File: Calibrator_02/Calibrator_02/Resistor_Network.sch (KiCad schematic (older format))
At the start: 61 parts, among them J6 Conn_Coaxial, U11 KAQY214STLD, U12 KAQY214STLD, U13 KAQY214STLD, U14 KAQY214STLD, U15 KAQY214STLD, U16 KAQY214STLD, U17 KAQY214STLD, U18 KAQY214STLD, U19 KAQY214STLD, U20 KAQY214STLD, U21 KAQY214STLD, U22 KAQY214STLD, U23 KAQY214STLD, U24 KAQY214STLD, U25 KAQY214STLD, U26 KAQY214STLD, U27 KAQY214STLD, U28 KAQY214STLD, U29 KAQY214STLD, U30 KAQY214STLD, U31 KAQY214STLD, U32 KAQY214STLD, U33 KAQY214STLD, U34 KAQY214STLD

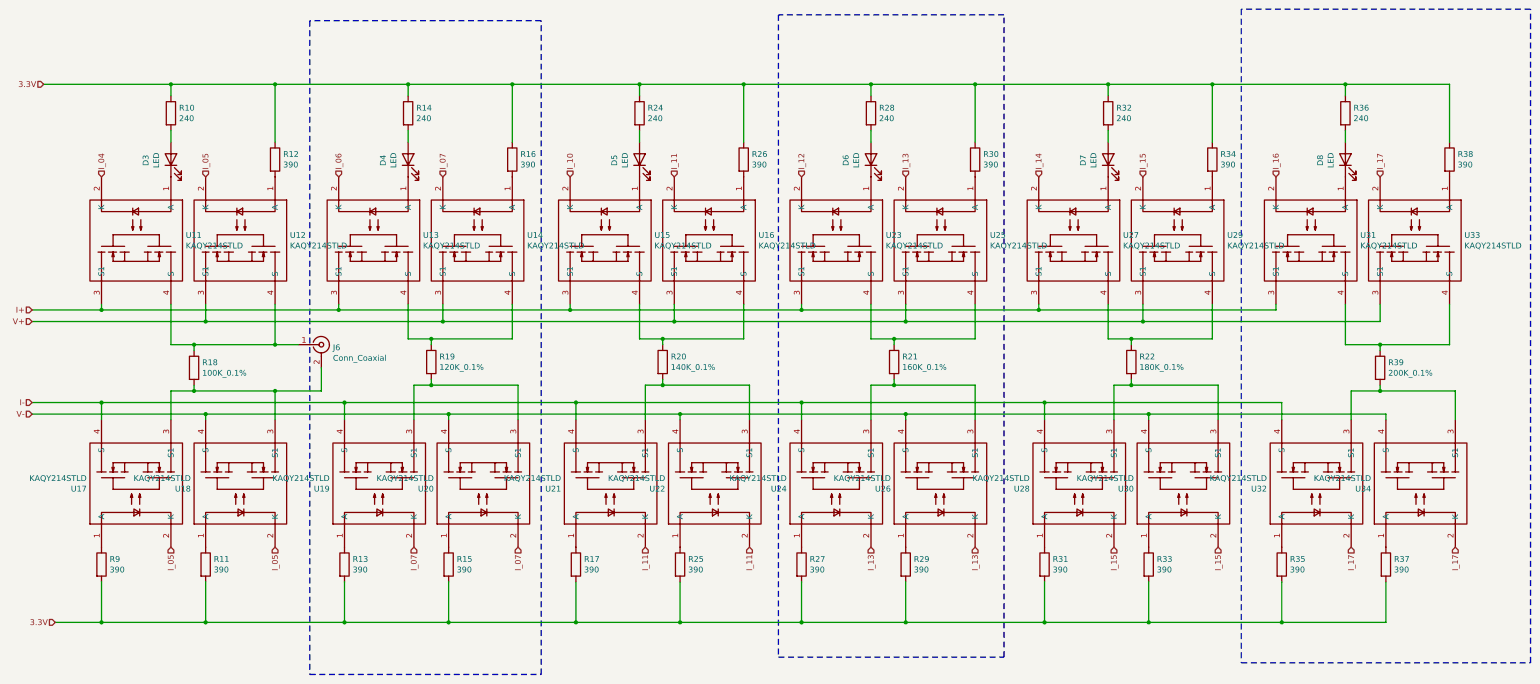
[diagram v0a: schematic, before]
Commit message: Fixed jst pinouts and made Cali board
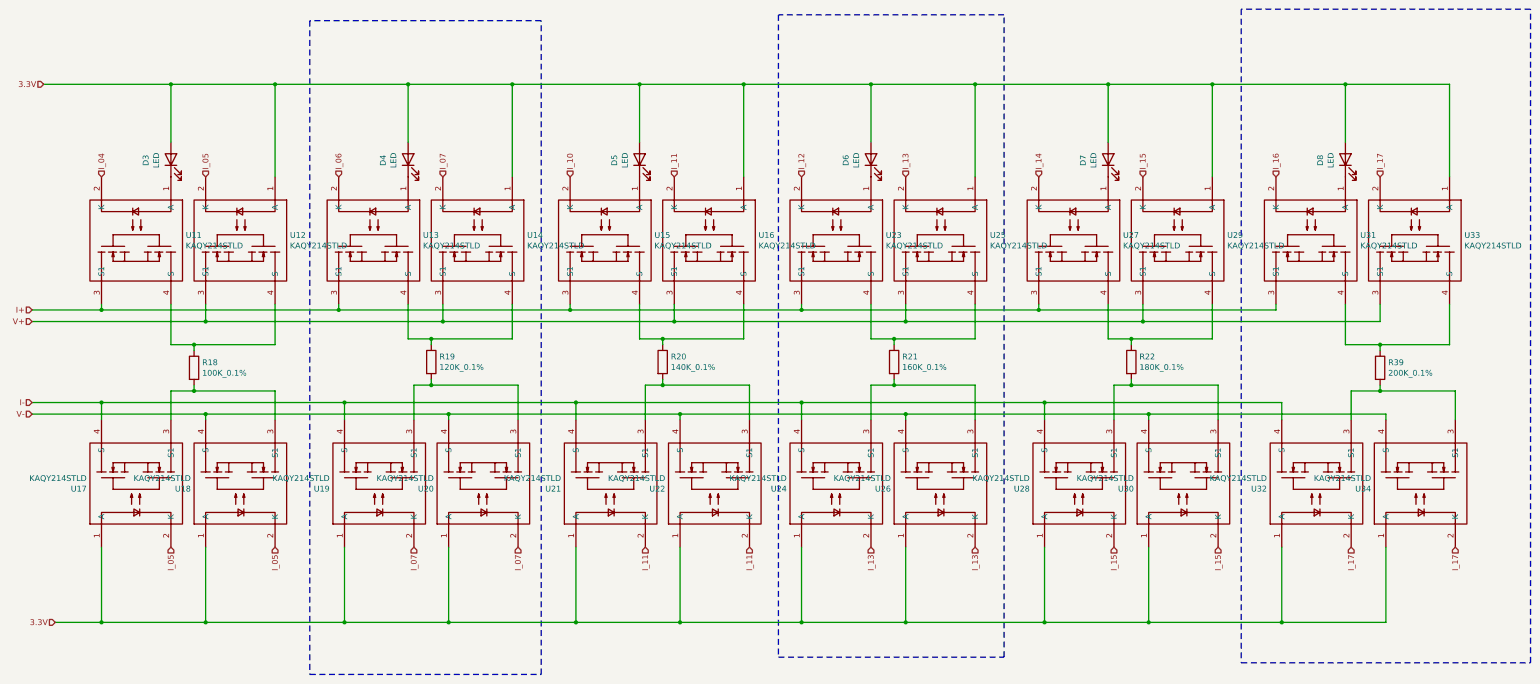
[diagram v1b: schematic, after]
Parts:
- removed J6: Conn_Coaxial, Connector_Coaxial:SMA_Amphenol_132134-10_Vertical, symbol Connector:Conn_Coaxial
- removed R10, R14, R24, R28, R32, R36: 240, Resistor_SMD:R_0402_1005Metric, symbol Device:R
- removed R11, R12, R13, R15, R16, R17, R25, R26, R27, R29, R30, R31, R33, R34, R35, R37, R38, R9: 390, Resistor_SMD:R_0603_1608Metric, symbol Device:R
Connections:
- net 3.3V: now also D3.2 (A), D4.2 (A), D5.2 (A), D6.2 (A), D7.2 (A), D8.2 (A), U12.1 (A), U14.1 (A), U16.1 (A), U17.1 (A), U18.1 (A), U19.1 (A), U20.1 (A), U21.1 (A), U22.1 (A), U24.1 (A), U25.1 (A), U26.1 (A), U28.1 (A), U29.1 (A), U30.1 (A), U32.1 (A), U33.1 (A), U34.1 (A)

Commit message: Update
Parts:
- renumbered R19 to R4, R20 to R5, R21 to R6, R22 to R7, R18 to R8, R39 to R9, U12 to U10, U13 to U11, U14 to U12, U15 to U13, U16 to U14, U23 to U15, U25 to U16, U27 to U17, U29 to U18, U31 to U19, U33 to U20, U17 to U21, U18 to U22, U19 to U23, U20 to U24, U21 to U25, U22 to U26, U24 to U27, U26 to U28, U28 to U29, U32 to U31, U34 to U32, U11 to U9
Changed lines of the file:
@@
 I_06
 $Comp
-L 0_Resistor02:KAQY214STLD U12
+L 0_Resistor02:KAQY214STLD U10
 U 1 1 62893971
 P 2450 2150
-F 0 "U12" V 2404 2578 50  0000 L CNN
+F 0 "U10" V 2404 2578 50  0000 L CNN
 F 1 "KAQY214STLD" V 2495 2578 50  0000 L CNN
 F 2 "0_Resistor_02:SOP-4_L3.9-W4.4-P2.54-LS7.0-BR" H 2450 2455 50  0001 C CNN
@@
 $EndComp
 $Comp
-L 0_Resistor02:KAQY214STLD U13
+L 0_Resistor02:KAQY214STLD U11
 U 1 1 62894BC4
 P 3600 2150
-F 0 "U13" V 3554 2578 50  0000 L CNN
+F 0 "U11" V 3554 2578 50  0000 L CNN
 F 1 "KAQY214STLD" V 3645 2578 50  0000 L CNN
 F 2 "0_Resistor_02:SOP-4_L3.9-W4.4-P2.54-LS7.0-BR" H 3600 2455 50  0001 C CNN
@@
 $EndComp
 $Comp
-L 0_Resistor02:KAQY214STLD U14
+L 0_Resistor02:KAQY214STLD U12
 U 1 1 6289536E
 P 4500 2150
-F 0 "U14" V 4454 2578 50  0000 L CNN
+F 0 "U12" V 4454 2578 50  0000 L CNN
 F 1 "KAQY214STLD" V 4545 2578 50  0000 L CNN
 F 2 "0_Resistor_02:SOP-4_L3.9-W4.4-P2.54-LS7.0-BR" H 4500 2455 50  0001 C CNN
@@
 $EndComp
 $Comp
-L 0_Resistor02:KAQY214STLD U16
+L 0_Resistor02:KAQY214STLD U14
 U 1 1 62898241
 P 6500 2150
-F 0 "U16" V 6454 2578 50  0000 L CNN
+F 0 "U14" V 6454 2578 50  0000 L CNN
 F 1 "KAQY214STLD" V 6545 2578 50  0000 L CNN
 F 2 "0_Resistor_02:SOP-4_L3.9-W4.4-P2.54-LS7.0-BR" H 6500 2455 50  0001 C CNN
@@
 $EndComp
 $Comp
-L 0_Resistor02:KAQY214STLD U15
+L 0_Resistor02:KAQY214STLD U13
 U 1 1 6289ADD7
 P 5600 2150
-F 0 "U15" V 5554 2578 50  0000 L CNN
+F 0 "U13" V 5554 2578 50  0000 L CNN
 F 1 "KAQY214STLD" V 5645 2578 50  0000 L CNN
 F 2 "0_Resistor_02:SOP-4_L3.9-W4.4-P2.54-LS7.0-BR" H 5600 2455 50  0001 C CNN
@@
 V-
 $Comp
-L 0_Resistor02:KAQY214STLD U17
+L 0_Resistor02:KAQY214STLD U21
 U 1 1 628C2DB7
 P 1550 4250
-F 0 "U17" V 1504 4678 50  0000 L CNN
+F 0 "U21" V 1504 4678 50  0000 L CNN
 F 1 "KAQY214STLD" V 1595 4678 50  0000 L CNN
 F 2 "0_Resistor_02:SOP-4_L3.9-W4.4-P2.54-LS7.0-BR" H 1550 4555 50  0001 C CNN
@@
 $EndComp
 $Comp
-L 0_Resistor02:KAQY214STLD U18
+L 0_Resistor02:KAQY214STLD U22
 U 1 1 628DB7E0
 P 2450 4250
-F 0 "U18" V 2404 4678 50  0000 L CNN
+F 0 "U22" V 2404 4678 50  0000 L CNN
 F 1 "KAQY214STLD" V 2495 4678 50  0000 L CNN
 F 2 "0_Resistor_02:SOP-4_L3.9-W4.4-P2.54-LS7.0-BR" H 2450 4555 50  0001 C CNN
@@
 $EndComp
 $Comp
-L 0_Resistor02:KAQY214STLD U25
+L 0_Resistor02:KAQY214STLD U16
 U 1 1 629247FB
 P 8500 2150
-F 0 "U25" V 8454 2578 50  0000 L CNN
+F 0 "U16" V 8454 2578 50  0000 L CNN
 F 1 "KAQY214STLD" V 8545 2578 50  0000 L CNN
 F 2 "0_Resistor_02:SOP-4_L3.9-W4.4-P2.54-LS7.0-BR" H 8500 2455 50  0001 C CNN
@@
 $EndComp
 $Comp
-L 0_Resistor02:KAQY214STLD U23
+L 0_Resistor02:KAQY214STLD U15
 U 1 1 62924803
 P 7600 2150
-F 0 "U23" V 7554 2578 50  0000 L CNN
+F 0 "U15" V 7554 2578 50  0000 L CNN
 F 1 "KAQY214STLD" V 7645 2578 50  0000 L CNN
 F 2 "0_Resistor_02:SOP-4_L3.9-W4.4-P2.54-LS7.0-BR" H 7600 2455 50  0001 C CNN
@@
 $EndComp
 $Comp
-L 0_Resistor02:KAQY214STLD U29
+L 0_Resistor02:KAQY214STLD U18
 U 1 1 6292807F
 P 10550 2150
-F 0 "U29" V 10504 2578 50  0000 L CNN
+F 0 "U18" V 10504 2578 50  0000 L CNN
 F 1 "KAQY214STLD" V 10595 2578 50  0000 L CNN
 F 2 "0_Resistor_02:SOP-4_L3.9-W4.4-P2.54-LS7.0-BR" H 10550 2455 50  0001 C CNN
@@
 $EndComp
 $Comp
-L 0_Resistor02:KAQY214STLD U27
+L 0_Resistor02:KAQY214STLD U17
 U 1 1 62928087
 P 9650 2150
-F 0 "U27" V 9604 2578 50  0000 L CNN
+F 0 "U17" V 9604 2578 50  0000 L CNN
 F 1 "KAQY214STLD" V 9695 2578 50  0000 L CNN
 F 2 "0_Resistor_02:SOP-4_L3.9-W4.4-P2.54-LS7.0-BR" H 9650 2455 50  0001 C CNN
@@
 $EndComp
 $Comp
-L 0_Resistor02:KAQY214STLD U19
+L 0_Resistor02:KAQY214STLD U23
 U 1 1 62952522
 P 3650 4250
-F 0 "U19" V 3604 4678 50  0000 L CNN
+F 0 "U23" V 3604 4678 50  0000 L CNN
 F 1 "KAQY214STLD" V 3695 4678 50  0000 L CNN
 F 2 "0_Resistor_02:SOP-4_L3.9-W4.4-P2.54-LS7.0-BR" H 3650 4555 50  0001 C CNN
@@
 $EndComp
 $Comp
-L 0_Resistor02:KAQY214STLD U20
+L 0_Resistor02:KAQY214STLD U24
 U 1 1 6295252A
 P 4550 4250
-F 0 "U20" V 4504 4678 50  0000 L CNN
+F 0 "U24" V 4504 4678 50  0000 L CNN
 F 1 "KAQY214STLD" V 4595 4678 50  0000 L CNN
 F 2 "0_Resistor_02:SOP-4_L3.9-W4.4-P2.54-LS7.0-BR" H 4550 4555 50  0001 C CNN
@@
 $EndComp
 $Comp
-L 0_Resistor02:KAQY214STLD U21
+L 0_Resistor02:KAQY214STLD U25
 U 1 1 6295A4E4
 P 5650 4250
-F 0 "U21" V 5604 4678 50  0000 L CNN
+F 0 "U25" V 5604 4678 50  0000 L CNN
 F 1 "KAQY214STLD" V 5695 4678 50  0000 L CNN
 F 2 "0_Resistor_02:SOP-4_L3.9-W4.4-P2.54-LS7.0-BR" H 5650 4555 50  0001 C CNN
@@
 $EndComp
 $Comp
-L 0_Resistor02:KAQY214STLD U22
+L 0_Resistor02:KAQY214STLD U26
 U 1 1 6295A4EC
 P 6550 4250
-F 0 "U22" V 6504 4678 50  0000 L CNN
+F 0 "U26" V 6504 4678 50  0000 L CNN
 F 1 "KAQY214STLD" V 6595 4678 50  0000 L CNN
 F 2 "0_Resistor_02:SOP-4_L3.9-W4.4-P2.54-LS7.0-BR" H 6550 4555 50  0001 C CNN
@@
 $EndComp
 $Comp
-L 0_Resistor02:KAQY214STLD U24
+L 0_Resistor02:KAQY214STLD U27
 U 1 1 6296491F
 P 7600 4250
-F 0 "U24" V 7554 4678 50  0000 L CNN
+F 0 "U27" V 7554 4678 50  0000 L CNN
 F 1 "KAQY214STLD" V 7645 4678 50  0000 L CNN
 F 2 "0_Resistor_02:SOP-4_L3.9-W4.4-P2.54-LS7.0-BR" H 7600 4555 50  0001 C CNN
@@
 $EndComp
 $Comp
-L 0_Resistor02:KAQY214STLD U26
+L 0_Resistor02:KAQY214STLD U28
 U 1 1 62964927
 P 8500 4250
-F 0 "U26" V 8454 4678 50  0000 L CNN
+F 0 "U28" V 8454 4678 50  0000 L CNN
 F 1 "KAQY214STLD" V 8545 4678 50  0000 L CNN
 F 2 "0_Resistor_02:SOP-4_L3.9-W4.4-P2.54-LS7.0-BR" H 8500 4555 50  0001 C CNN
@@
 $EndComp
 $Comp
-L 0_Resistor02:KAQY214STLD U28
+L 0_Resistor02:KAQY214STLD U29
 U 1 1 62969201
 P 9700 4250
-F 0 "U28" V 9654 4678 50  0000 L CNN
+F 0 "U29" V 9654 4678 50  0000 L CNN
 F 1 "KAQY214STLD" V 9745 4678 50  0000 L CNN
 F 2 "0_Resistor_02:SOP-4_L3.9-W4.4-P2.54-LS7.0-BR" H 9700 4555 50  0001 C CNN
@@
 Connection ~ 7300 2750
 $Comp
-L 0_Resistor02:KAQY214STLD U33
+L 0_Resistor02:KAQY214STLD U20
 U 1 1 62985DC3
 P 12600 2150
-F 0 "U33" V 12554 2578 50  0000 L CNN
+F 0 "U20" V 12554 2578 50  0000 L CNN
 F 1 "KAQY214STLD" V 12645 2578 50  0000 L CNN
 F 2 "0_Resistor_02:SOP-4_L3.9-W4.4-P2.54-LS7.0-BR" H 12600 2455 50  0001 C CNN
@@
 $EndComp
 $Comp
-L 0_Resistor02:KAQY214STLD U31
+L 0_Resistor02:KAQY214STLD U19
 U 1 1 62985DCB
 P 11700 2150
-F 0 "U31" V 11654 2578 50  0000 L CNN
+F 0 "U19" V 11654 2578 50  0000 L CNN
 F 1 "KAQY214STLD" V 11745 2578 50  0000 L CNN
 F 2 "0_Resistor_02:SOP-4_L3.9-W4.4-P2.54-LS7.0-BR" H 11700 2455 50  0001 C CNN
@@
 $EndComp
 $Comp
-L 0_Resistor02:KAQY214STLD U32
+L 0_Resistor02:KAQY214STLD U31
 U 1 1 62985DF2
 P 11750 4250
-F 0 "U32" V 11704 4678 50  0000 L CNN
+F 0 "U31" V 11704 4678 50  0000 L CNN
 F 1 "KAQY214STLD" V 11795 4678 50  0000 L CNN
 F 2 "0_Resistor_02:SOP-4_L3.9-W4.4-P2.54-LS7.0-BR" H 11750 4555 50  0001 C CNN
@@
 $EndComp
 $Comp
-L 0_Resistor02:KAQY214STLD U34
+L 0_Resistor02:KAQY214STLD U32
 U 1 1 62985DFA
 P 12650 4250
-F 0 "U34" V 12604 4678 50  0000 L CNN
+F 0 "U32" V 12604 4678 50  0000 L CNN
 F 1 "KAQY214STLD" V 12695 4678 50  0000 L CNN
 F 2 "0_Resistor_02:SOP-4_L3.9-W4.4-P2.54-LS7.0-BR" H 12650 4555 50  0001 C CNN
@@
 	11400 2750 11400 2700
 $Comp
-L 0_Resistor02:KAQY214STLD U11
+L 0_Resistor02:KAQY214STLD U9
 U 1 1 6288E641
 P 1550 2150
-F 0 "U11" V 1504 2578 50  0000 L CNN
+F 0 "U9" V 1504 2578 50  0000 L CNN
 F 1 "KAQY214STLD" V 1595 2578 50  0000 L CNN
 F 2 "0_Resistor_02:SOP-4_L3.9-W4.4-P2.54-LS7.0-BR" H 1550 2455 50  0001 C CNN
@@
 $EndComp
 $Comp
-L Device:R R39
+L Device:R R9
 U 1 1 6298B64E
 P 12300 3250
-F 0 "R39" H 12370 3296 50  0000 L CNN
+F 0 "R9" H 12370 3296 50  0000 L CNN
 F 1 "200K_0.1%" H 12370 3205 50  0000 L CNN
 F 2 "Resistor_SMD:R_0603_1608Metric_Pad0.98x0.95mm_HandSolder" V 12230 3250 50  0001 C CNN
@@
 	12300 3450 12950 3450
 $Comp
-L Device:R R22
+L Device:R R7
 U 1 1 6299B156
 P 10150 3200
-F 0 "R22" H 10220 3246 50  0000 L CNN
+F 0 "R7" H 10220 3246 50  0000 L CNN
 F 1 "180K_0.1%" H 10220 3155 50  0000 L CNN
 F 2 "Resistor_SMD:R_0805_2012Metric_Pad1.20x1.40mm_HandSolder" V 10080 3200 50  0001 C CNN
@@
 	10150 3400 10900 3400
 $Comp
-L Device:R R21
+L Device:R R6
 U 1 1 629A9E7C
 P 8100 3200
-F 0 "R21" H 8170 3246 50  0000 L CNN
+F 0 "R6" H 8170 3246 50  0000 L CNN
 F 1 "160K_0.1%" H 8170 3155 50  0000 L CNN
 F 2 "Resistor_SMD:R_0805_2012Metric_Pad1.20x1.40mm_HandSolder" V 8030 3200 50  0001 C CNN
@@
 	8100 3400 8800 3400
 $Comp
-L Device:R R20
+L Device:R R5
 U 1 1 629B9198
 P 6100 3200
-F 0 "R20" H 6170 3246 50  0000 L CNN
+F 0 "R5" H 6170 3246 50  0000 L CNN
 F 1 "140K_0.1%" H 6170 3155 50  0000 L CNN
 F 2 "Resistor_SMD:R_0603_1608Metric_Pad0.98x0.95mm_HandSolder" V 6030 3200 50  0001 C CNN
@@
 	6100 3400 6850 3400
 $Comp
-L Device:R R19
+L Device:R R4
 U 1 1 629C927A
 P 4100 3200
-F 0 "R19" H 4170 3246 50  0000 L CNN
+F 0 "R4" H 4170 3246 50  0000 L CNN
 F 1 "120K_0.1%" H 4170 3155 50  0000 L CNN
 F 2 "Resistor_SMD:R_0603_1608Metric_Pad0.98x0.95mm_HandSolder" V 4030 3200 50  0001 C CNN
@@
 	4100 3400 4850 3400
 $Comp
-L Device:R R18
+L Device:R R8
 U 1 1 629D9115
 P 2050 3250
-F 0 "R18" H 2120 3296 50  0000 L CNN
+F 0 "R8" H 2120 3296 50  0000 L CNN
 F 1 "100K_0.1%" H 2120 3205 50  0000 L CNN
 F 2 "Resistor_SMD:R_0603_1608Metric_Pad0.98x0.95mm_HandSolder" V 1980 3250 50  0001 C CNN

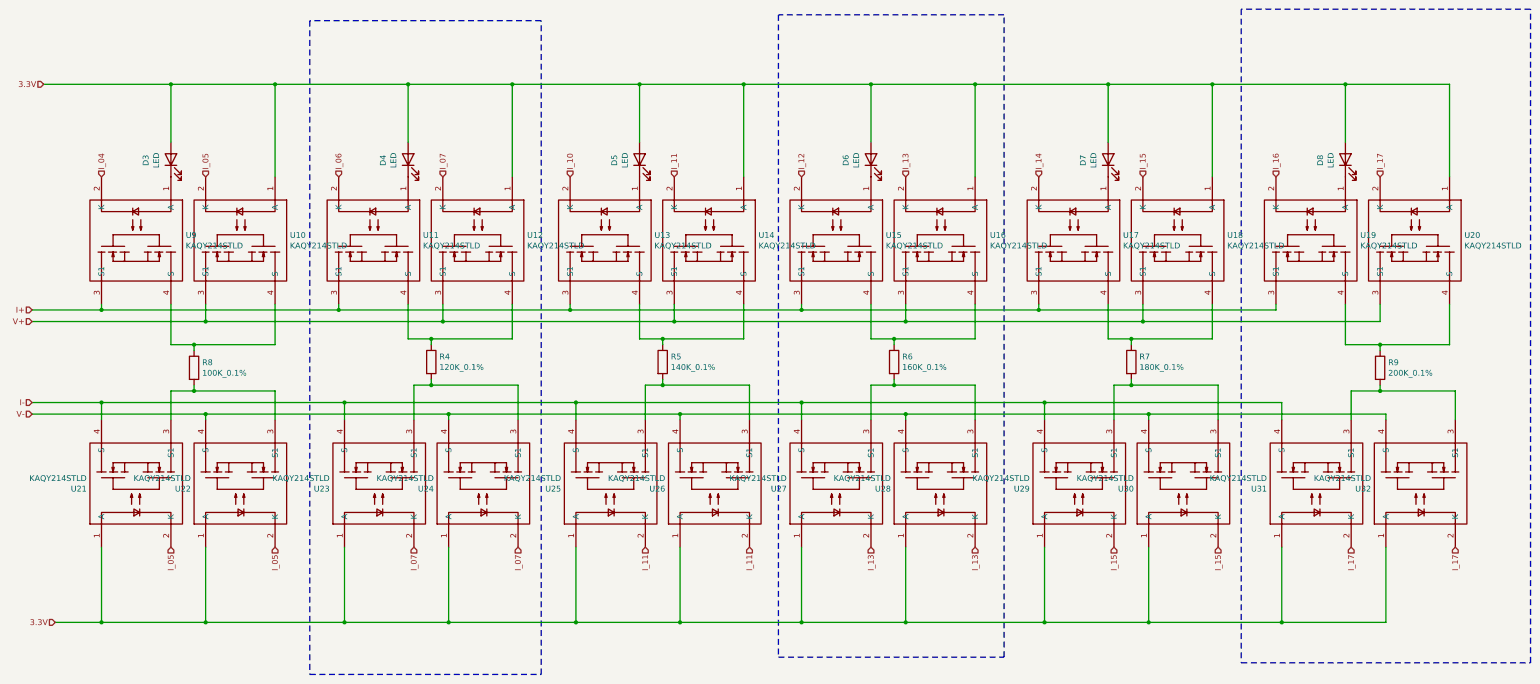
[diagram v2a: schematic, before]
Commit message: Added Resistors to Diodes
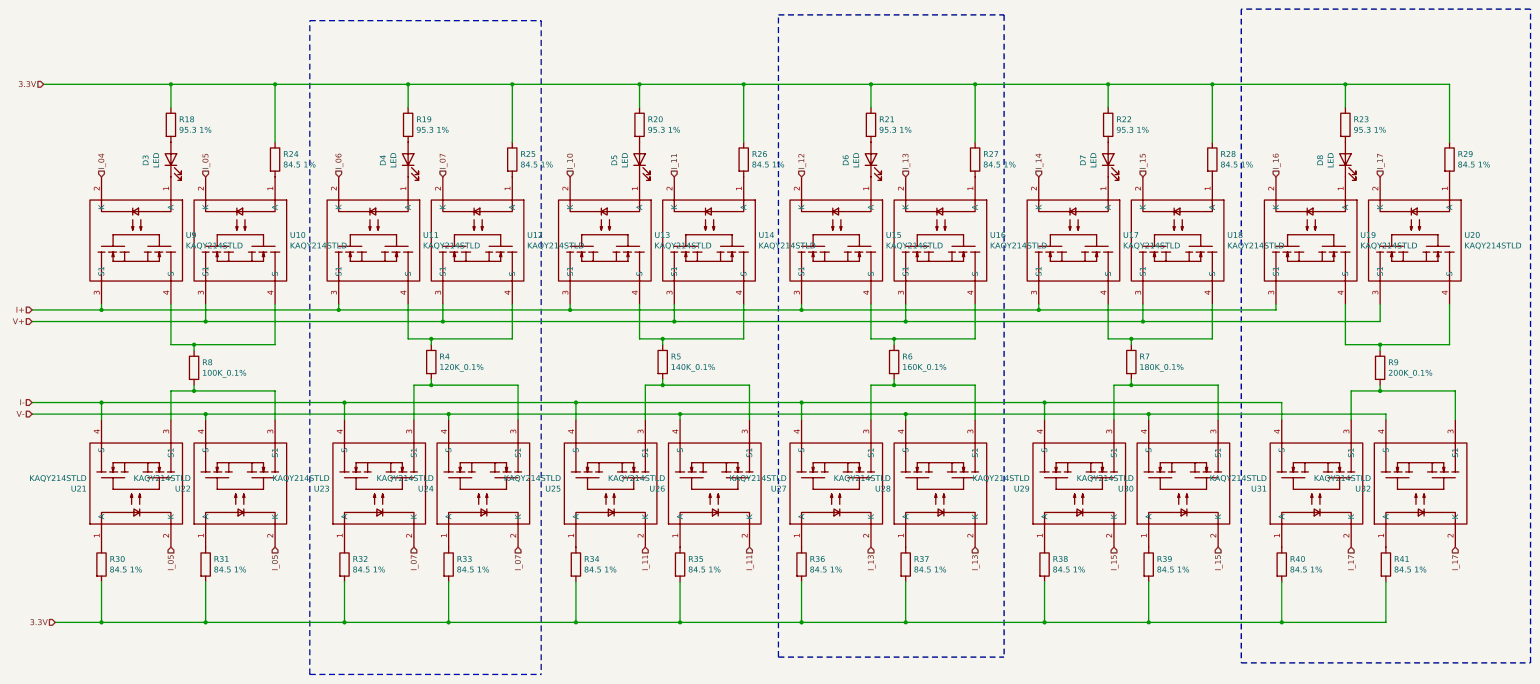
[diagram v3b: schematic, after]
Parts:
- added R18, R19, R20, R21, R22, R23: 95.3 1%, Resistor_SMD:R_0201_0603Metric_Pad0.64x0.40mm_HandSolder, symbol Device:R
- added R24, R25, R26, R27, R28, R29, R30, R31, R32, R33, R34, R35, R36, R37, R38, R39, R40, R41: 84.5 1%, Resistor_SMD:R_0201_0603Metric_Pad0.64x0.40mm_HandSolder, symbol Device:R
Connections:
- net 3.3V: now also R18.1, R19.1, R20.1, R21.1, R22.1, R23.1, R24.1, R25.1, R26.1, R27.1, R28.1, R29.1, R30.2, R31.2, R32.2, R33.2, R34.2, R35.2, R36.2, R37.2, R38.2, R39.2, R40.2, R41.2; no longer D3.2 (A), D4.2 (A), D5.2 (A), D6.2 (A), D7.2 (A), D8.2 (A), U10.1 (A), U12.1 (A), U14.1 (A), U16.1 (A), U18.1 (A), U20.1 (A), U21.1 (A), U22.1 (A), U23.1 (A), U24.1 (A), U25.1 (A), U26.1 (A), U27.1 (A), U28.1 (A), U29.1 (A), U30.1 (A), U31.1 (A), U32.1 (A)
- new net: D3.2 (A), R18.2
- new net: D8.2 (A), R23.2
- new net: D7.2 (A), R22.2
- new net: D6.2 (A), R21.2
- new net: D5.2 (A), R20.2
- new net: D4.2 (A), R19.2
- new net: R24.2, U10.1 (A)
- new net: R25.2, U12.1 (A)
- new net: R26.2, U14.1 (A)
- new net: R27.2, U16.1 (A)
- new net: R28.2, U18.1 (A)
- new net: R29.2, U20.1 (A)
- new net: R41.1, U32.1 (A)
- new net: R40.1, U31.1 (A)
- new net: R39.1, U30.1 (A)
- new net: R38.1, U29.1 (A)
- new net: R37.1, U28.1 (A)
- new net: R36.1, U27.1 (A)
- new net: R35.1, U26.1 (A)
- new net: R34.1, U25.1 (A)
- new net: R33.1, U24.1 (A)
- new net: R32.1, U23.1 (A)
- new net: R30.1, U21.1 (A)
- new net: R31.1, U22.1 (A)
